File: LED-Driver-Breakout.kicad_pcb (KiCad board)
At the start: 6 copper layers, 98 x 100 mm, 17 parts, among them J1 S2B-XH-A, J2 LED Output, J3 XT60, J4 01x03_PinHeaderSwitch, U1 V10P45-M3/86A, U2 TSR2-24120

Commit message: did layout, still need to fix ERC errors and DRC warnings
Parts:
- added DRIVER_V_IN1: TestPoint, TestPoint:TestPoint_Loop_D2.54mm_Drill1.5mm_Beaded, F.Cu at (145.9, 125.7)
- added GND: MountingHole_3.2mm_M3_Pad_Via, MountingHole:MountingHole_3.2mm_M3_Pad_Via, F.Cu at (145.0, 135.0)
- added GND1: TestPoint, TestPoint:TestPoint_Loop_D2.54mm_Drill1.5mm_Beaded, F.Cu at (145.9, 64.7)
- added REF**: MountingHole_3.2mm_M3_Pad_Via, MountingHole:MountingHole_3.2mm_M3_Pad_Via, F.Cu at (65.0, 55.0)
- added REF**: MountingHole_3.2mm_M3_Pad_Via, MountingHole:MountingHole_3.2mm_M3_Pad_Via, F.Cu at (145.0, 55.0)
- added REF**: MountingHole_3.2mm_M3_Pad_Via, MountingHole:MountingHole_3.2mm_M3_Pad_Via, F.Cu at (65.0, 135.0)
- added REGULATOR_IN1: TestPoint, TestPoint:TestPoint_Loop_D2.54mm_Drill1.5mm_Beaded, F.Cu at (145.9, 101.3)
- added SWITCH1: TestPoint, TestPoint:TestPoint_Loop_D2.54mm_Drill1.5mm_Beaded, F.Cu at (145.9, 76.9)
- added V_FUSED1: TestPoint, TestPoint:TestPoint_Loop_D2.54mm_Drill1.5mm_Beaded, F.Cu at (145.9, 89.1)
- added V_REGULATED1: TestPoint, TestPoint:TestPoint_Loop_D2.54mm_Drill1.5mm_Beaded, F.Cu at (145.9, 113.5)
- moved C1 78.3 mm to (107.9, 54.9), turned to -90 degrees
- moved C2 77.4 mm to (102.2, 54.7), turned to -90 degrees
- moved D1 72.3 mm to (71.5, 53.3), turned to -90 degrees
- moved R1 69.1 mm to (77.7, 53.0), turned to -90 degrees
- moved L1 36.1 mm to (75.7, 83.3)
- moved J4 34.5 mm to (62.2, 78.5)
- moved C3 32.4 mm to (69.6, 84.5), turned to -90 degrees
- moved C4 32.3 mm to (72.5, 84.5), turned to -90 degrees
- moved C6 31.0 mm to (78.8, 84.2), turned to -90 degrees
- moved J1 26.7 mm to (72.7, 110.3)
- moved U2 26.0 mm to (64.7, 98.9)
- moved PS1 25.5 mm to (114.0, 98.6)
- moved J2 24.6 mm to (68.8, 122.2)
- moved C5 24.6 mm to (73.9, 92.7), turned to 90 degrees
- moved U1 9.88 mm to (92.7, 56.8), turned to 180 degrees
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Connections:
- net /V_Fused renamed +24V
- net /switch renamed /SWITCH
- net Net-(U2-Vin) renamed /REGULATOR_V_IN
- net Net-(U2-Vout) renamed /V_REGULATED
- C1 pad 2: Net-(PS1-VIN-) -> /GND
- C2 pad 2: Net-(PS1-VIN-) -> /GND
- C3 pad 2: Net-(U2-GND) -> /GND
- C4 pad 2: Net-(U2-GND) -> /GND
- C5 pad 2: Net-(U2-GND) -> /GND
- C6 pad 2: Net-(U2-GND) -> /GND
- J3 pad 1: /GND -> Net-(J3-Pad1)
- J4 pad 1: /GND -> Net-(J4-Pin_1)
- PS1 pad 2: Net-(PS1-VIN-) -> /GND
- PS1 pad 3: /GND -> Net-(PS1-DIM-)
- U2 pad 2: Net-(U2-GND) -> /GND
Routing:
- net /REGULATOR_V_IN: track 0.00 -> 115.3 mm
- net /V_REGULATED: track 0.00 -> 100.8 mm
- net /SWITCH: track 0.00 -> 92.4 mm
- net /GND: track 0.00 -> 62.3 mm, vias 0 -> 4
- net Net-(PS1-VOUT+): track 13.7 -> 42.1 mm
- net Net-(PS1-VOUT-): track 0.00 -> 27.9 mm
- net Net-(D1-A): track 0.00 -> 6.28 mm
- net +24V: track 58.5 -> 63.5 mm, vias 0 -> 4
- net Net-(F1-Pad1): track 7.65 -> 6.52 mm
- net Net-(F1-Pad2): track 8.99 -> 8.15 mm
- added copper zone on In1.Cu, net +24V
- added copper zone on In2.Cu, net /GND
- removed copper zone on In2.Cu, net +24V
- removed copper zone on In1.Cu, net /GND
- removed copper zone on In4.Cu, net /GND
- removed copper zone on In3.Cu, net /V_REGULATED
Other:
- board size 98 x 100 mm -> 90 x 90 mm
- copper layers 6 -> 4

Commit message: Tiny updates.
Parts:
- removed DRIVER_V_IN1: TestPoint, TestPoint:TestPoint_Loop_D2.54mm_Drill1.5mm_Beaded
- removed U2: TSR2-24120, Converter_DCDC:Converter_DCDC_TRACO_TSR2-xxxx_THT
- added U3: TSR2-24120, Converter_DCDC:Converter_DCDC_TRACO_TSR2-xxxx_THT, F.Cu at (64.5, 98.6)
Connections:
- GND1 pad 1: Net-(GND1-Pad1) -> /GND
- J1 pad 2: Net-(U2-GND) -> /GND
- J3 pad 1: Net-(J3-Pad1) -> /GND
- J4 pad 1: Net-(J4-Pin_1) -> /GND
- PS1 pad 3: Net-(PS1-DIM-) -> unconnected-(PS1-DIM--Pad3)

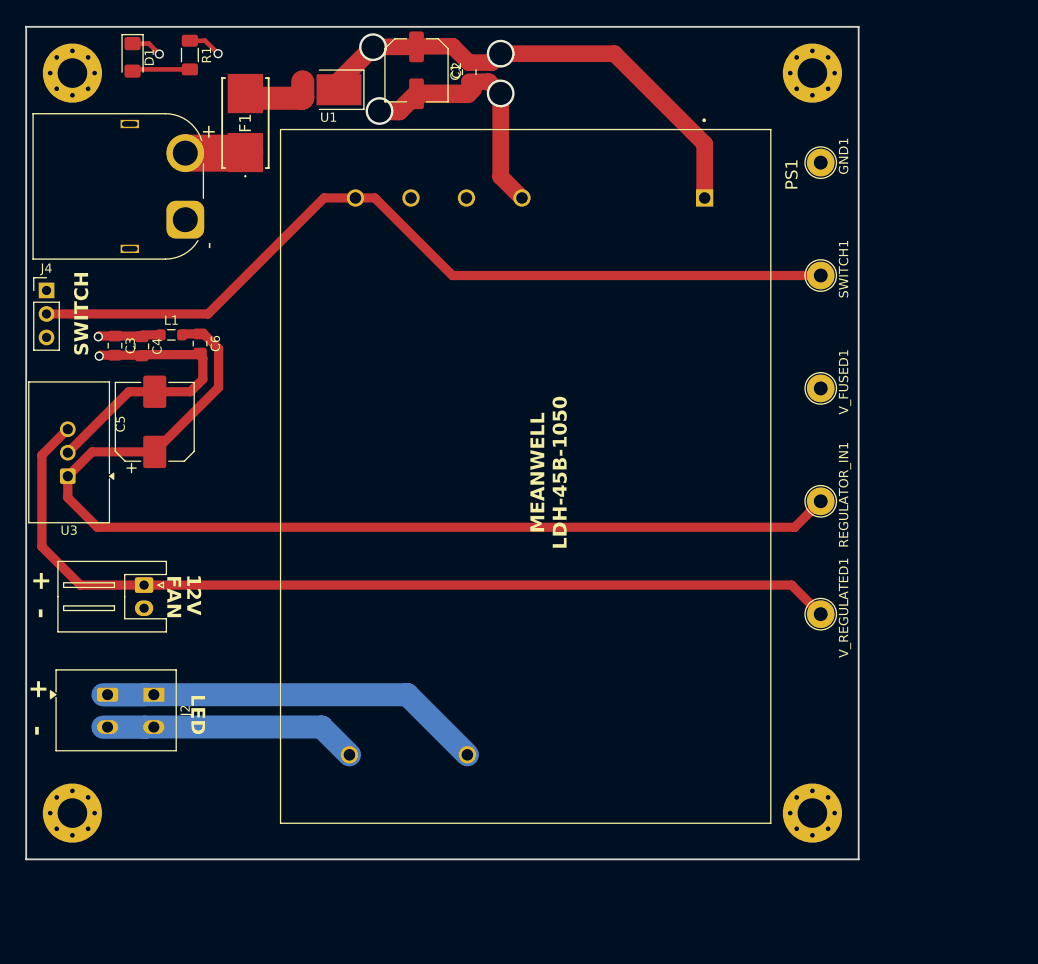
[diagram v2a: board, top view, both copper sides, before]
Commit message: Minor edits to layout to allow passing of ERC.
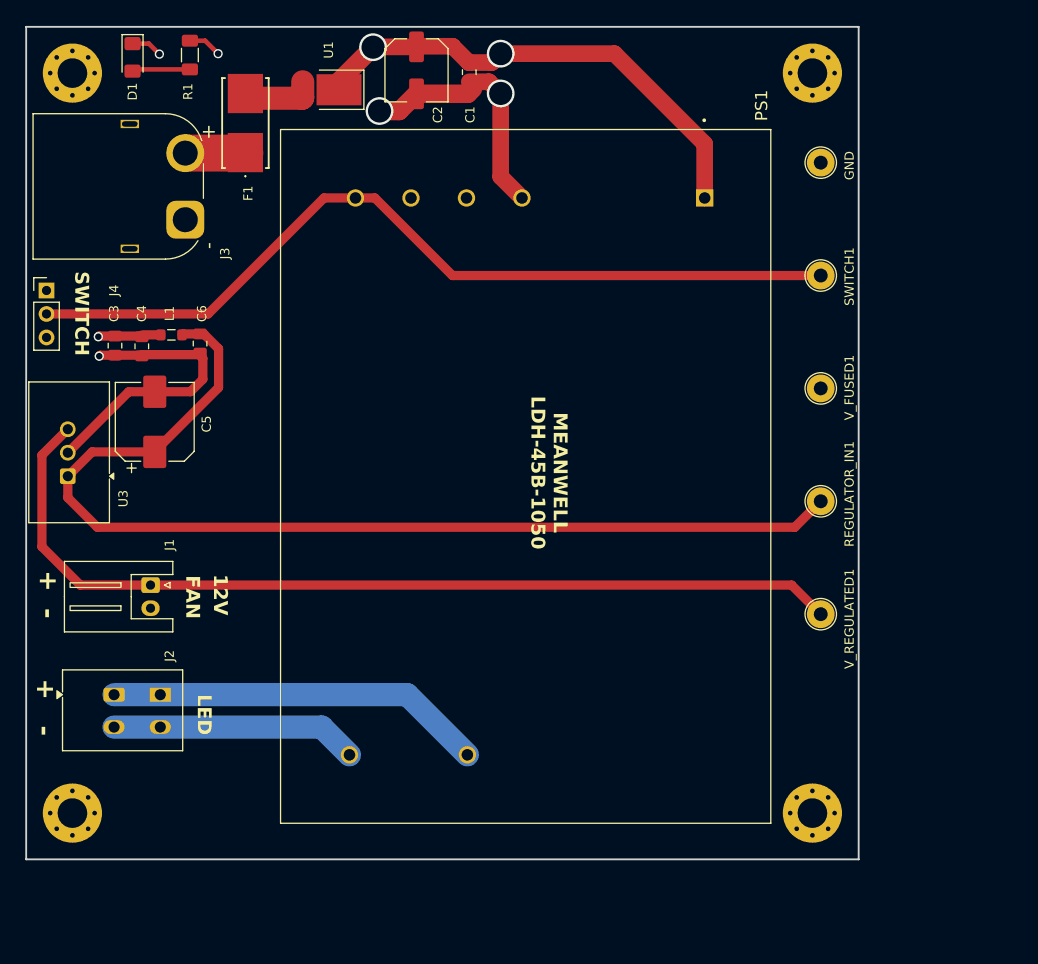
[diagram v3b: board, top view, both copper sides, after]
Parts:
- moved J2 0.70 mm to (69.5, 122.2)
- moved J1 0.70 mm to (73.4, 110.3)
- renumbered GND1 to GND
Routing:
- net Net-(PS1-VOUT-): track 27.9 -> 26.7 mm
- net Net-(PS1-VOUT+): track 42.1 -> 40.9 mm

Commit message: added back deisgn
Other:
- board text removed: "45W LED Driver Breakout"
